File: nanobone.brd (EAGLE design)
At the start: 30.5 x 30.5 mm, 44 parts, among them J1 USD_CONNECTOR, U1 24LC_32AT-I/OT, U2 OSD3358, U3 SN74LVC1G07_DCK_5, U4 AR8035-AL1B, Y1 CM200C-32.768KAZF-UT, Y2 445C33D24M00000

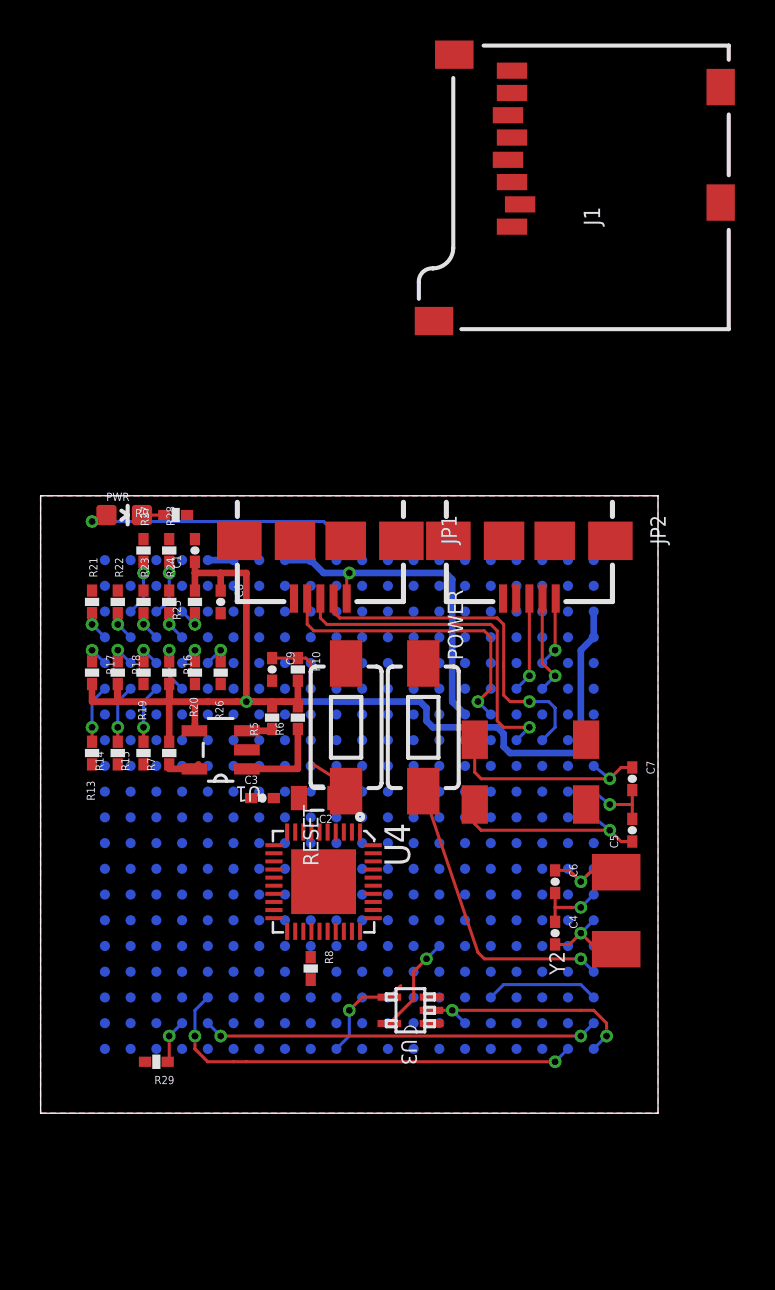
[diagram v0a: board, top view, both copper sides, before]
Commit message: Removed AR8035 due to lack of space and routing issues. Centered crystals in pocketbone.lbr and renamed to nanobone.lbr
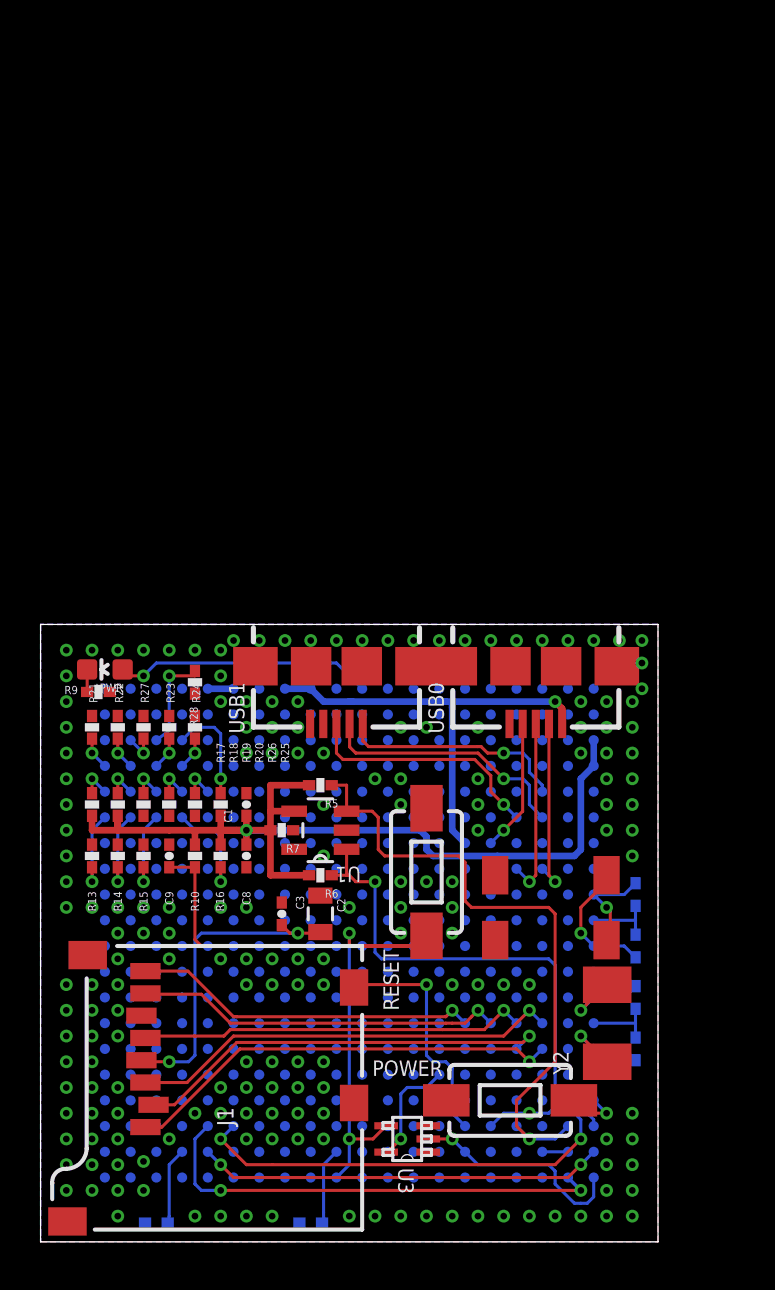
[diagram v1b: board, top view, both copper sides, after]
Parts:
- removed JP1, JP2: (no value), pocketbone:USB-AB-MICRO-SMD
- removed U4: AR8035-AL1B, AR8035-AL1B:QFN40P500X500X75-41N
- added USB0, USB1: (no value), pocketbone:USB-AB-MICRO-SMD
- moved J1 48.0 mm to (15.9, 14.6)
- moved POWER 18.9 mm to (23.2, 6.99), turned to 0 degrees
- moved C1 12.8 mm to (10.2, 21.6)
- moved C8 12.6 mm to (10.2, 19.1)
- moved R8 12.5 mm to (13.3, 0.95), flipped to the bottom, turned to 180 degrees
- moved C9 10.5 mm to (6.35, 19.1), turned to 90 degrees
- moved R10 10.5 mm to (7.62, 19.1), turned to 90 degrees
- moved R25 10.1 mm to (8.89, 21.6), turned to 270 degrees
- moved R9 9.53 mm to (2.86, 27.1)
- moved R16 9.40 mm to (8.89, 19.1), turned to 90 degrees
- moved R27 8.73 mm to (5.08, 25.4)
- moved RESET 8.17 mm to (19.1, 18.3)
- moved R29 7.94 mm to (5.71, 0.95), flipped to the bottom, turned to 0 degrees
- moved R6 7.86 mm to (13.8, 18.1), turned to 180 degrees
- moved PWR 7.68 mm to (3.17, 28.3), turned to 90 degrees
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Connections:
- removed net AVDD33: U4.14
- removed net AVDDL: U4.11, U4.17, U4.6
- removed net DVDDL: U4.38
- removed net N$14: U4.9
- removed net N$15: U4.12
- removed net N$16: U4.15
- removed net N$17: U4.18
- removed net N$18: U4.33
- removed net N$19: U4.10
- removed net N$20: U4.13
- removed net N$21: U4.16
- removed net N$22: U4.19
- removed net N$23: U4.27
- removed net N$24: U4.8
- removed net N$7: U4.41
- removed net VDD33: U4.3
- net GND: now also USB0.GND, USB0.SHIELD1, USB0.SHIELD2, USB0.SHIELD3, USB0.SHIELD4, USB1.GND, USB1.SHIELD1, USB1.SHIELD2, USB1.SHIELD3, USB1.SHIELD4; no longer JP1.GND, JP1.SHIELD1, JP1.SHIELD2, JP1.SHIELD3, JP1.SHIELD4, JP2.GND, JP2.SHIELD1, JP2.SHIELD2, JP2.SHIELD3, JP2.SHIELD4
- net MDC: no longer U4.40
- net MII1_RXD0: no longer U4.29
- net MII1_RXD1: no longer U4.28
- net MII1_RXD2: no longer U4.26
- net MII1_RXD3: no longer U4.25
- net MII1_RX_CLK: no longer U4.31
- net MII1_RX_DV: no longer U4.30
- net MII1_TXD0: no longer U4.34
- net MII1_TXD1: no longer U4.35
- net MII1_TXD2: no longer U4.36
- net MII1_TXD3: no longer U4.37
- net MII1_TX_EN: no longer U4.32
- net N$1: now also USB1.D+; no longer JP2.D+
- net N$4: now also USB1.D-; no longer JP2.D-
- net N$6: now also USB1.VBUS; no longer JP2.VBUS
- net USB0_DM: now also USB0.D-; no longer JP1.D-
- net USB0_DP: now also USB0.D+; no longer JP1.D+
- net USB0_ID: now also USB0.ID; no longer JP1.ID
- net USB_DC: now also USB0.VBUS; no longer JP1.VBUS
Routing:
- net I2C0_SDA: track 1.33 -> 31.7 mm, vias 0 -> 1
- net N$12: track 0.00 -> 21.9 mm, vias 0 -> 2
- net NTE: track 0.00 -> 21.7 mm, vias 0 -> 1
- net N$74: track 0.00 -> 21.3 mm, vias 0 -> 1
- net RESET: track 14.6 -> 35.8 mm, vias 1 -> 2
- net N$5: track 0.00 -> 20.9 mm, vias 0 -> 1
- net I2C0_SCL: track 10.1 -> 30.2 mm, vias 0 -> 2
- net N$2: track 0.00 -> 19.3 mm, vias 0 -> 1
- net N$77: track 0.00 -> 18.4 mm, vias 0 -> 1
- net N$70: track 0.00 -> 17.2 mm, vias 0 -> 1
- net VCC_3V3B: track 0.00 -> 16.4 mm, vias 0 -> 2
- net N$75: track 0.00 -> 12.1 mm, vias 0 -> 1
- net PWR: track 14.5 -> 3.01 mm
- net USB0_DM: track 17.5 -> 8.81 mm
- net USB0_ID: track 14.9 -> 6.53 mm
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
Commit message: Smash names and cleaned up for visibility
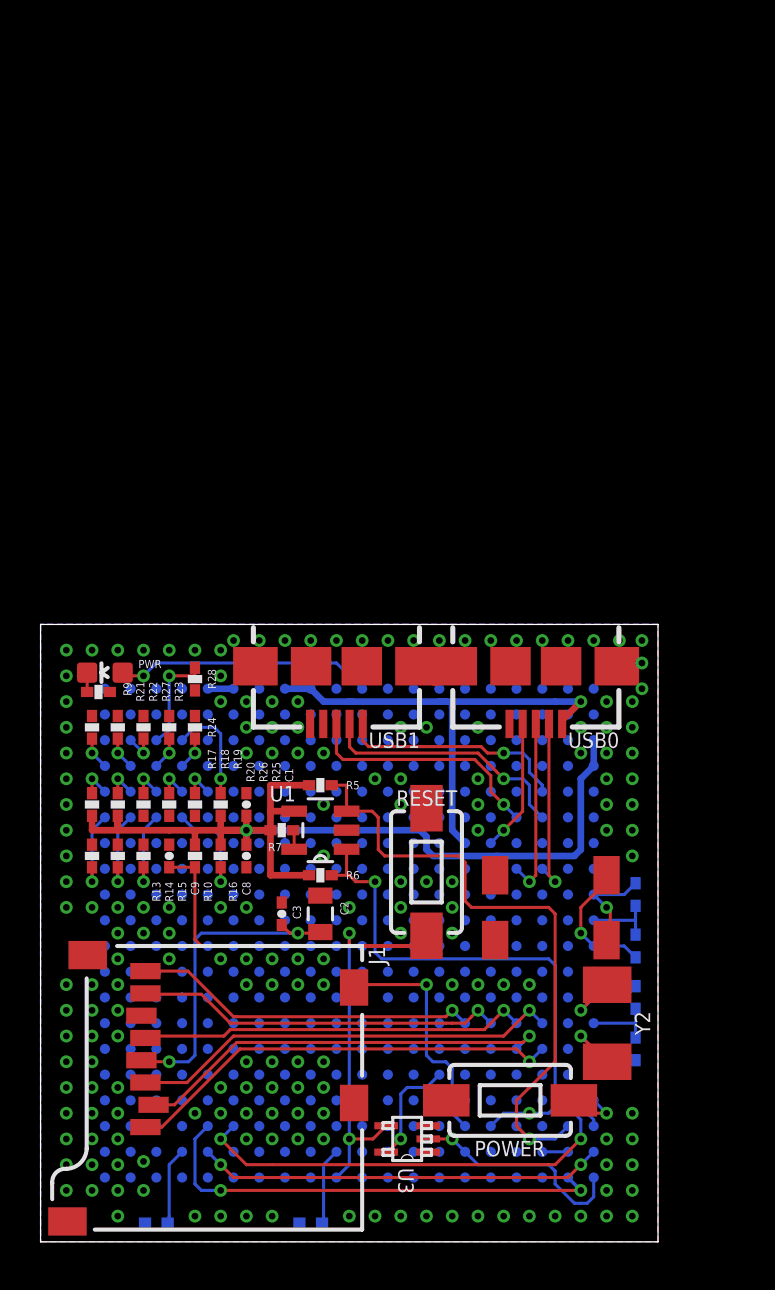
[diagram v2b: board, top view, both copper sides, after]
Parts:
- moved PWR 0.16 mm to (3.17, 28.1)
- moved R28 0.16 mm to (7.62, 27.8)
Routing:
- net USB_DC: track 22.7 -> 24.2 mm
- net N$28: track 0.00 -> 0.99 mm

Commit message: Remove PHY nets from schematic. Tie all DGND to GND plane. Improve USB differential pair isolation.
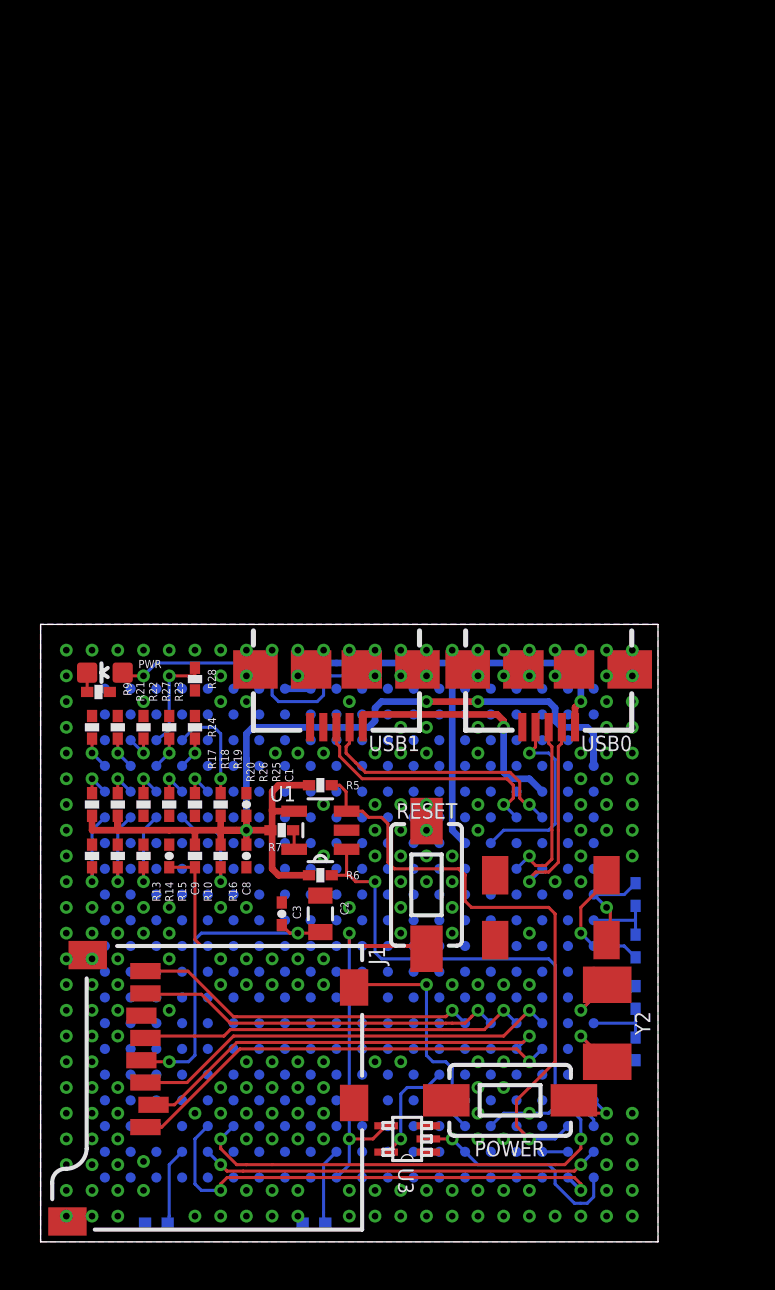
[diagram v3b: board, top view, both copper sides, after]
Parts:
- moved USB0 0.65 mm to (25.1, 28.3)
- moved RESET 0.64 mm to (19.1, 17.6)
- moved USB1 0.16 mm to (14.6, 28.3)
- moved R8 0.16 mm to (13.5, 0.95)
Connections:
- removed net 5.0V: U2.Y5, U2.Y6
- removed net MDC: U2.M18
- removed net MDIO: U2.M17
- removed net MII1_COL: U2.H16
- removed net MII1_CRS: U2.H17
- removed net MII1_REF_CLK: U2.H18
- removed net MII1_RXD0: U2.M16
- removed net MII1_RXD1: U2.L15
- removed net MII1_RXD2: U2.L16
- removed net MII1_RXD3: U2.L17
- removed net MII1_RX_CLK: U2.L18
- removed net MII1_RX_DV: U2.J17
- removed net MII1_RX_ER: U2.J15
- removed net MII1_TXD0: U2.K17
- removed net MII1_TXD1: U2.K16
- removed net MII1_TXD2: U2.K15
- removed net MII1_TXD3: U2.J18
- removed net MII1_TX_CLK: U2.K18
- removed net MII1_TX_EN: U2.J16
- new net VIN_AC_0: U2.Y5
- new net VIN_AC_1: U2.Y6
- net GND: now also U2.A18, U2.E19, U2.E20, U2.F19, U2.F8, U2.G11, U2.G12, U2.G19, U2.G8, U2.G9, U2.H10, U2.H12, U2.H19, U2.H6, U2.H7, U2.H8, U2.H9, U2.J10, U2.J11, U2.J19, U2.J20, U2.J7, U2.J8, U2.J9, U2.K10, U2.K11, U2.K19, U2.K7, U2.K9, U2.L10, U2.L11, U2.L12, U2.L13, U2.M12, U2.M14, U2.M6, U2.M7, U2.M8, U2.M9, U2.N10, U2.N11, U2.N14, U2.N19, U2.N20, U2.P19, U2.P20, U2.R19, U2.R20, U2.T19, U2.T20, U2.U19, U2.V18, U2.W10, U2.W12, U2.W13, U2.W14, U2.W15, U2.W16, U2.W17, U2.W18, U2.W19, U2.W3, U2.W5, U2.W6, U2.W7, U2.W8, U2.W9, U2.Y10, U2.Y12, U2.Y15, U2.Y7
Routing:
- net USB_DC: track 24.2 -> 27.9 mm
- net USB0_ID: track 6.53 -> 9.55 mm
- net 3.3V: track 49.7 -> 52.2 mm, vias 1 -> 3
- net VDD_3V3AUX: track 12.8 -> 14.9 mm
- net 5.0V: track 1.27 -> 0.00 mm
- net N$6: track 11.3 -> 12.6 mm
- net PMIC_NWAKEUP: track 24.1 -> 25.3 mm
- net USB0_DM: track 8.81 -> 9.84 mm
- net N$1: track 12.1 -> 12.8 mm
- net N$12: track 21.9 -> 22.5 mm

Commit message: Cleaned layout further, added USB1_ID, added user LEDs
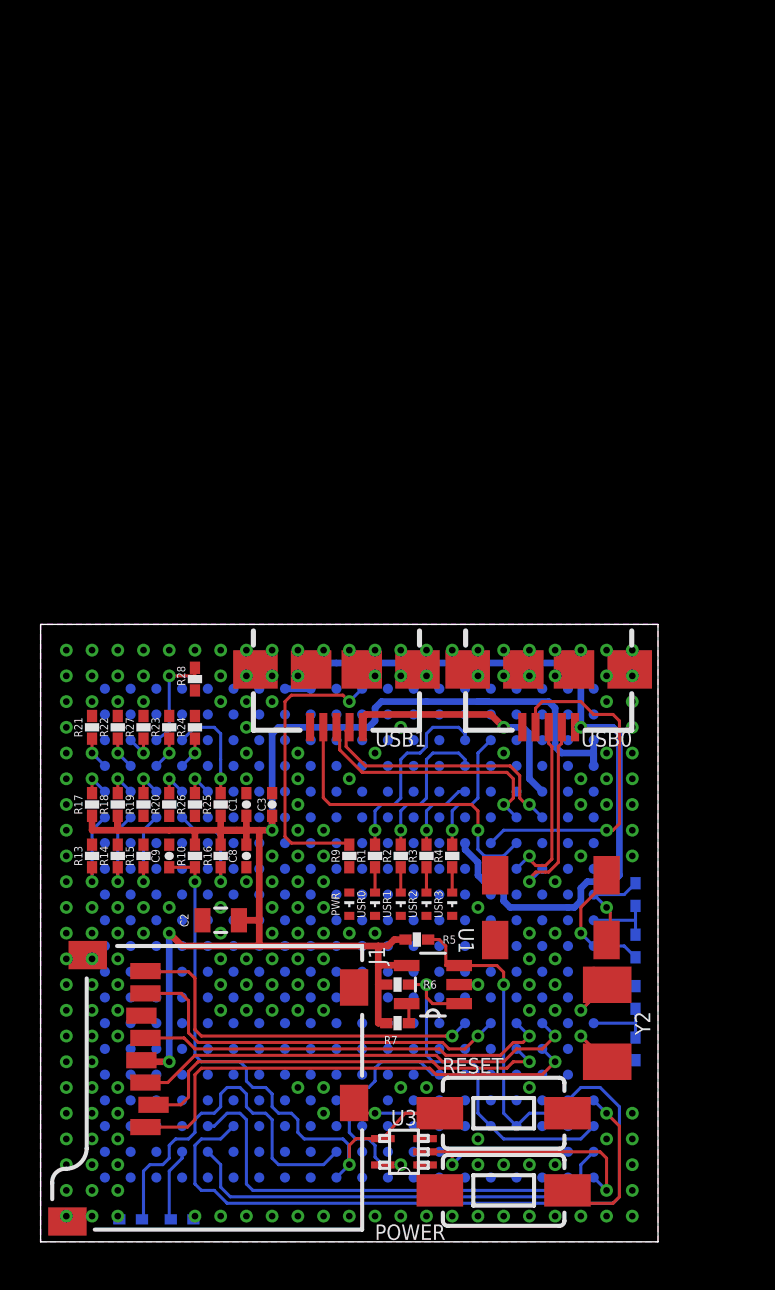
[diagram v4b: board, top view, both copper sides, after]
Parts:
- added R1, R2, R3, R4: 240, Strawson_Eagle_Lib:0402-RES
- added USR0, USR1, USR2, USR3: BLUE, nanobone:0402-LED
- PWR: device BeagleBone_Blue:LED-0603 -> nanobone:0402-LED
- moved PWR 16.6 mm to (15.2, 16.7), turned to 270 degrees
- moved R9 14.8 mm to (15.2, 19.1), turned to 90 degrees
- moved RESET 11.9 mm to (22.9, 6.35), turned to 180 degrees
- moved R7 11.1 mm to (17.6, 10.8)
- moved U1 9.43 mm to (19.4, 12.7)
- moved R8 9.05 mm to (4.45, 1.11)
- moved R5 8.99 mm to (18.6, 14.9)
- moved R6 6.61 mm to (17.6, 12.7)
- moved C3 5.42 mm to (11.4, 21.6)
- moved C2 4.93 mm to (8.89, 15.9), turned to 0 degrees
- moved POWER 4.46 mm to (22.9, 2.54)
- moved R29 1.28 mm to (6.99, 1.11), turned to 180 degrees
- moved U3 0.65 mm to (17.9, 4.45)
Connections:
- removed net PWR_LEDR: PWR.C, R9.2
- removed net VCC_3V3B: C2.2, C3.2, J1.VCC
- new net N$10: R3.1, USR2.A
- new net N$11: R4.1, USR3.A
- new net N$13: PWR.A, R9.1
- new net N$8: R1.1, USR0.A
- new net N$9: R2.1, USR1.A
- new net USB1_ID: U2.P17, USB1.ID
- new net USR0: R1.2, U2.V15
- new net USR1: R2.2, U2.U15
- new net USR2: R3.2, U2.T15
- new net USR3: R4.2, U2.V16
- net 3.3V: now also C2.2, C3.2, J1.VCC
- net GND: now also PWR.C, USR0.C, USR1.C, USR2.C, USR3.C; no longer R9.1
- net N$75: now also J1.CD2; no longer J1.CD1
- net VDD_3V3AUX: now also R9.2; no longer PWR.A
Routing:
- net 3.3V: track 52.2 -> 76.6 mm
- net VCC_3V3B: track 16.4 -> 0.00 mm, vias 2 -> 0
- net I2C0_SDA: track 31.8 -> 15.9 mm
- net USB1_ID: track 0.00 -> 15.6 mm, vias 0 -> 1
- net N$7: track 3.84 -> 18.4 mm
- net I2C0_SCL: track 30.2 -> 18.3 mm, vias 2 -> 1
- net USB_DC: track 27.9 -> 39.5 mm
- net N$12: track 22.5 -> 33.3 mm, vias 2 -> 0
- net USR0: track 0.00 -> 9.76 mm, vias 0 -> 1
- net USB0_ID: track 9.55 -> 17.4 mm
- net USR1: track 0.00 -> 7.59 mm, vias 0 -> 1
- net VDD_RTC: track 5.59 -> 12.1 mm
- net USR3: track 0.00 -> 6.32 mm, vias 0 -> 1
- net N$75: track 12.1 -> 6.25 mm
- net PWR: track 3.01 -> 8.25 mm
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
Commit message: Fix µSD trace ground plane surround
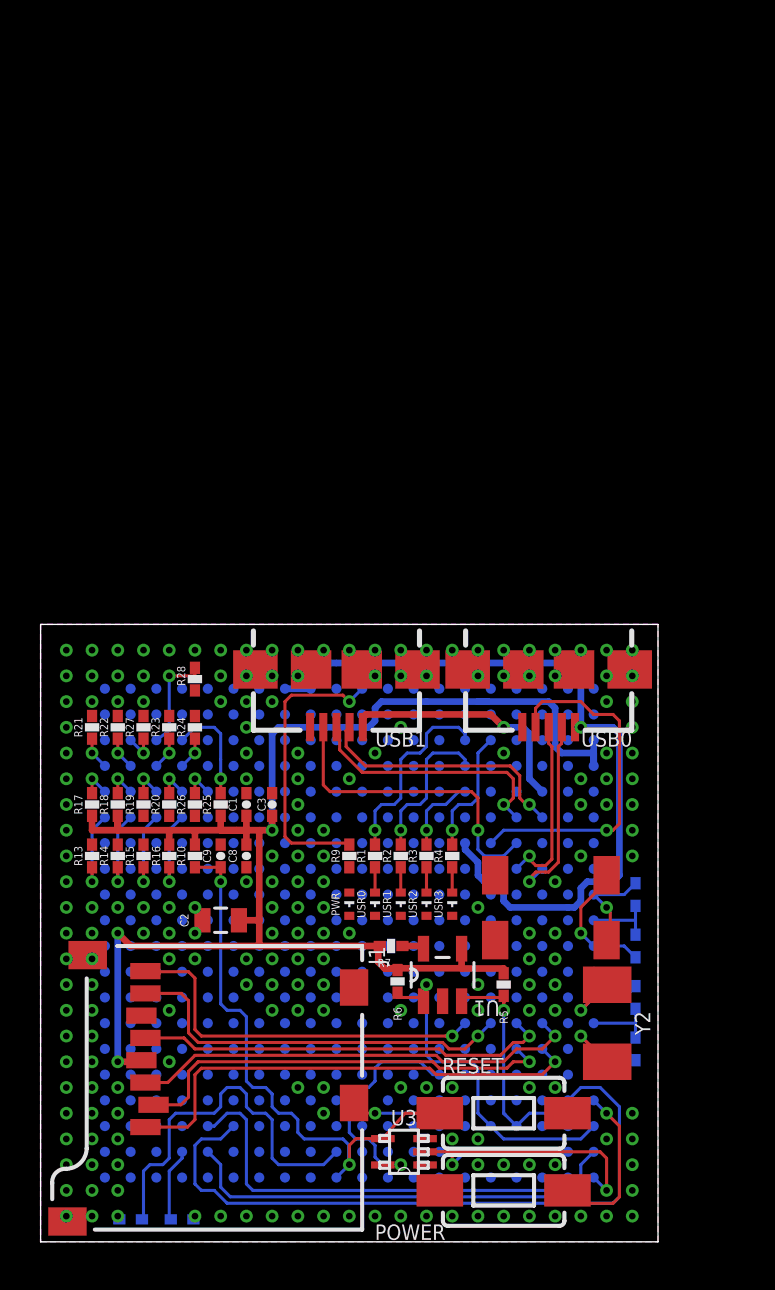
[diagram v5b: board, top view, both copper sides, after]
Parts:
- moved R5 4.83 mm to (22.9, 12.7), turned to 90 degrees
- moved R7 3.82 mm to (17.3, 14.6)
- moved C9 2.54 mm to (8.89, 19.1)
- moved R16 2.54 mm to (6.35, 19.1)
- moved U1 0.67 mm to (19.8, 13.2), turned to 90 degrees
- moved R6 0.16 mm to (17.6, 12.9), turned to 90 degrees
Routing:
- net 3.3V: track 76.6 -> 80.4 mm
- net I2C0_SDA: track 15.9 -> 13.2 mm
- net RESET: track 31.0 -> 29.7 mm
- net MDIR_3A: track 5.23 -> 4.15 mm
